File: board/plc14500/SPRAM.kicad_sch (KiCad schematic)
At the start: 26 parts, among them U12 4011, U13 4099, U14 4051

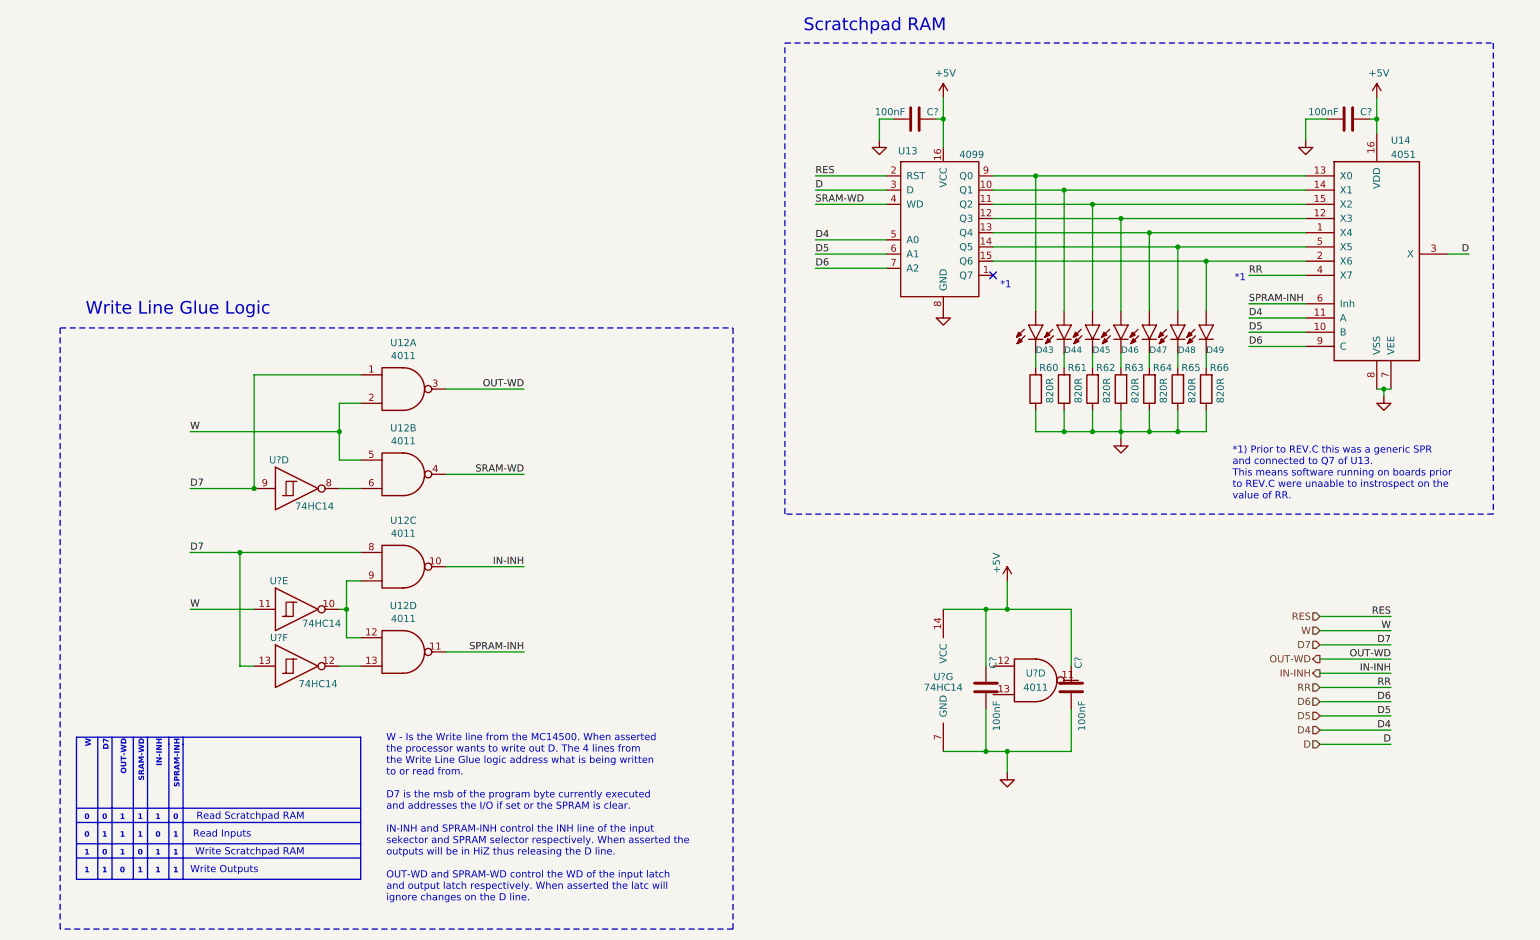
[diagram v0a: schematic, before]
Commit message: Address ERC errors
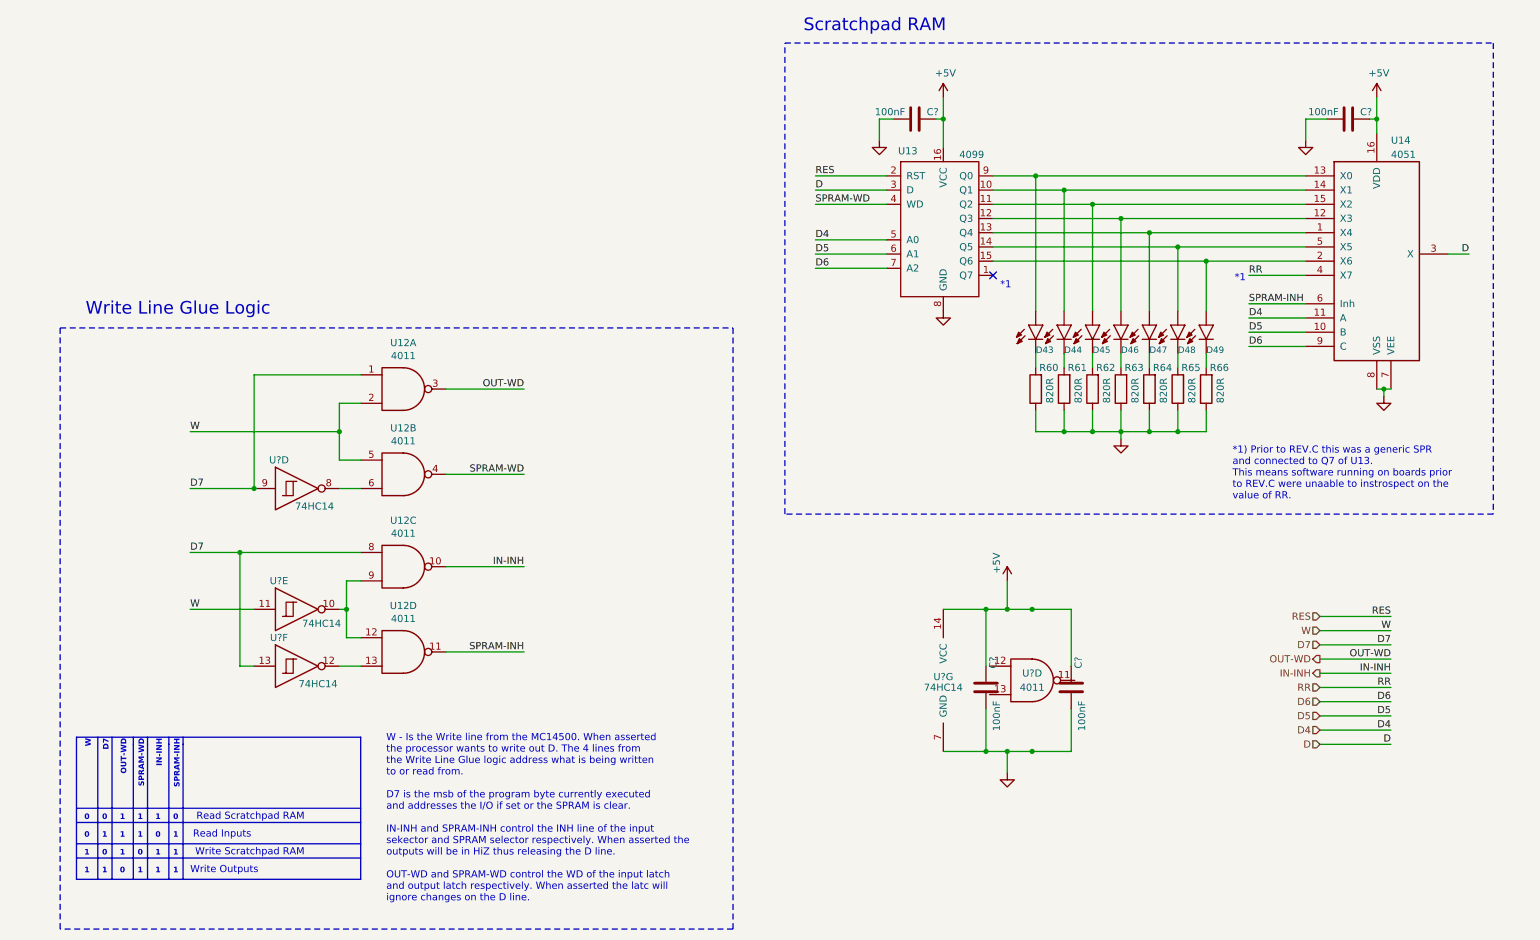
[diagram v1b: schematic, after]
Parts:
- D43, D44, D45, D46, D47, D48, D49: footprint plc14500:LED_3MM -> LED_5MM; symbol plc14500-rescue:LED5MM-SparkFun-LED -> plc14500:LED
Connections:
- net SRAM-WD renamed SPRAM-WD
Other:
- note added: "SPRAM-WD"
- note removed: "SRAM-WD"
- moved on the sheet: U?D
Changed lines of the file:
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@@
     (comment 1 "REV.D")
   )
+  (junction (at 198.755 149.86) (diameter 0) (color 0 0 0 0)
+  )
   (junction (at 214.63 92.71) (diameter 0) (color 0 0 0 0)
   )
@@
   )
   (junction (at 204.47 49.53) (diameter 0) (color 0 0 0 0)
+  )
+  (junction (at 198.755 124.46) (diameter 0) (color 0 0 0 0)
   )
   (junction (at 194.31 124.46) (diameter 0) (color 0 0 0 0)
@@
     (stroke (width 0) (type default))
   )
-  (wire (pts (xy 194.31 124.46) (xy 205.74 124.46))
+  (wire (pts (xy 194.31 124.46) (xy 198.755 124.46))
     (stroke (width 0) (type default))
   )
@@
     (stroke (width 0) (type default))
   )
-  (wire (pts (xy 194.31 149.86) (xy 205.74 149.86))
+  (wire (pts (xy 194.31 149.86) (xy 198.755 149.86))
     (stroke (width 0) (type default))
   )
@@
     (stroke (width 0) (type default))
   )
+  (wire (pts (xy 198.755 124.46) (xy 205.74 124.46))
+    (stroke (width 0) (type default))
+  )
   (wire (pts (xy 93.98 132.08) (xy 107.95 132.08))
     (stroke (width 0) (type default))
   )
   (wire (pts (xy 214.63 54.61) (xy 247.65 54.61))
+    (stroke (width 0) (type default))
+  )
+  (wire (pts (xy 198.755 149.86) (xy 205.74 149.86))
     (stroke (width 0) (type default))
   )
@@
     (effects (font (size 0.9906 0.9906) (thickness 0.1981) bold) (justify right bottom))
   )
-  (text "SRAM-WD" (at 40.132 147.701 90)
+  (text "SPRAM-WD" (at 40.132 147.701 90)
     (effects (font (size 0.9906 0.9906) (thickness 0.1981) bold) (justify right bottom))
   )
@@
     (effects (font (size 1.27 1.27)) (justify right bottom))
   )
-  (label "SRAM-WD" (at 160.02 52.07 0) (fields_autoplaced)
+  (label "SPRAM-WD" (at 160.02 52.07 0) (fields_autoplaced)
     (effects (font (size 1.27 1.27)) (justify left bottom))
   )
@@
     (effects (font (size 1.27 1.27)) (justify right bottom))
   )
-  (label "SRAM-WD" (at 107.95 100.33 180) (fields_autoplaced)
+  (label "SPRAM-WD" (at 107.95 100.33 180) (fields_autoplaced)
     (effects (font (size 1.27 1.27)) (justify right bottom))
   )
@@
     (effects (font (size 1.27 1.27)) (justify right))
   )
-  (symbol (lib_id "plc14500-rescue:LED5MM-SparkFun-LED") (at 199.39 73.66 0) (unit 1)
+  (symbol (lib_id "plc14500:LED") (at 199.39 73.66 0) (unit 1)
     (in_bom yes) (on_board yes) (dnp no)
     (property "Reference" "D43" (at 199.39 78.105 0)
@@
       (effects (font (size 1.143 1.143)) (justify left) hide)
     )
-    (property "Footprint" "plc14500:LED_3MM" (at 194.31 73.66 90)
+    (property "Footprint" "LED_5MM" (at 194.31 73.66 90)
       (effects (font (size 0.508 0.508)) hide)
     )
@@
       (effects (font (size 1.27 1.27)) hide)
     )
-    (property "Field4" "XXX-00000" (at 201.3712 77.0636 0)
-      (effects (font (size 1.524 1.524)) (justify left) hide)
+    (property "Field4" "XXX-00000" (at 193.04 73.66 90)
+      (effects (font (size 1.524 1.524)) hide)
     )
     (property "Price" "0.01" (at 199.39 73.66 0)
@@
     )
   )
-  (symbol (lib_id "plc14500-rescue:LED5MM-SparkFun-LED") (at 204.47 73.66 0) (unit 1)
+  (symbol (lib_id "plc14500:LED") (at 204.47 73.66 0) (unit 1)
     (in_bom yes) (on_board yes) (dnp no)
     (property "Reference" "D44" (at 204.47 78.105 0)
@@
       (effects (font (size 1.143 1.143)) (justify left) hide)
     )
-    (property "Footprint" "plc14500:LED_3MM" (at 199.39 73.66 90)
+    (property "Footprint" "LED_5MM" (at 199.39 73.66 90)
       (effects (font (size 0.508 0.508)) hide)
     )
@@
       (effects (font (size 1.27 1.27)) hide)
     )
-    (property "Field4" "XXX-00000" (at 206.4512 77.0636 0)
-      (effects (font (size 1.524 1.524)) (justify left) hide)
+    (property "Field4" "XXX-00000" (at 198.12 73.66 90)
+      (effects (font (size 1.524 1.524)) hide)
     )
     (property "Price" "0.01" (at 204.47 73.66 0)
@@
     )
   )
-  (symbol (lib_id "plc14500-rescue:LED5MM-SparkFun-LED") (at 209.55 73.66 0) (unit 1)
+  (symbol (lib_id "plc14500:LED") (at 209.55 73.66 0) (unit 1)
     (in_bom yes) (on_board yes) (dnp no)
     (property "Reference" "D45" (at 209.55 78.105 0)
@@
       (effects (font (size 1.143 1.143)) (justify left) hide)
     )
-    (property "Footprint" "plc14500:LED_3MM" (at 204.47 73.66 90)
+    (property "Footprint" "LED_5MM" (at 204.47 73.66 90)
       (effects (font (size 0.508 0.508)) hide)
     )
@@
       (effects (font (size 1.27 1.27)) hide)
     )
-    (property "Field4" "XXX-00000" (at 211.5312 77.0636 0)
-      (effects (font (size 1.524 1.524)) (justify left) hide)
+    (property "Field4" "XXX-00000" (at 203.2 73.66 90)
+      (effects (font (size 1.524 1.524)) hide)
     )
     (property "Price" "0.01" (at 209.55 73.66 0)
@@
     )
   )
-  (symbol (lib_id "plc14500-rescue:LED5MM-SparkFun-LED") (at 214.63 73.66 0) (unit 1)
+  (symbol (lib_id "plc14500:LED") (at 214.63 73.66 0) (unit 1)
     (in_bom yes) (on_board yes) (dnp no)
     (property "Reference" "D46" (at 214.63 78.105 0)
@@
       (effects (font (size 1.143 1.143)) (justify left) hide)
     )
-    (property "Footprint" "plc14500:LED_3MM" (at 209.55 73.66 90)
+    (property "Footprint" "LED_5MM" (at 209.55 73.66 90)
       (effects (font (size 0.508 0.508)) hide)
     )
@@
       (effects (font (size 1.27 1.27)) hide)
     )
-    (property "Field4" "XXX-00000" (at 216.6112 77.0636 0)
-      (effects (font (size 1.524 1.524)) (justify left) hide)
+    (property "Field4" "XXX-00000" (at 208.28 73.66 90)
+      (effects (font (size 1.524 1.524)) hide)
     )
     (property "Price" "0.01" (at 214.63 73.66 0)
@@
     )
   )
-  (symbol (lib_id "plc14500-rescue:LED5MM-SparkFun-LED") (at 219.71 73.66 0) (unit 1)
+  (symbol (lib_id "plc14500:LED") (at 219.71 73.66 0) (unit 1)
     (in_bom yes) (on_board yes) (dnp no)
     (property "Reference" "D47" (at 219.71 78.105 0)
@@
       (effects (font (size 1.143 1.143)) (justify left) hide)
     )
-    (property "Footprint" "plc14500:LED_3MM" (at 214.63 73.66 90)
+    (property "Footprint" "LED_5MM" (at 214.63 73.66 90)
       (effects (font (size 0.508 0.508)) hide)
     )
@@
       (effects (font (size 1.27 1.27)) hide)
     )
-    (property "Field4" "XXX-00000" (at 221.6912 77.0636 0)
-      (effects (font (size 1.524 1.524)) (justify left) hide)
+    (property "Field4" "XXX-00000" (at 213.36 73.66 90)
+      (effects (font (size 1.524 1.524)) hide)
     )
     (property "Price" "0.01" (at 219.71 73.66 0)
@@
     )
   )
-  (symbol (lib_id "plc14500-rescue:LED5MM-SparkFun-LED") (at 224.79 73.66 0) (unit 1)
+  (symbol (lib_id "plc14500:LED") (at 224.79 73.66 0) (unit 1)
     (in_bom yes) (on_board yes) (dnp no)
     (property "Reference" "D48" (at 224.79 78.105 0)
@@
       (effects (font (size 1.143 1.143)) (justify left) hide)
     )
-    (property "Footprint" "plc14500:LED_3MM" (at 219.71 73.66 90)
+    (property "Footprint" "LED_5MM" (at 219.71 73.66 90)
       (effects (font (size 0.508 0.508)) hide)
     )
@@
       (effects (font (size 1.27 1.27)) hide)
     )
-    (property "Field4" "XXX-00000" (at 226.7712 77.0636 0)
-      (effects (font (size 1.524 1.524)) (justify left) hide)
+    (property "Field4" "XXX-00000" (at 218.44 73.66 90)
+      (effects (font (size 1.524 1.524)) hide)
     )
     (property "Price" "0.01" (at 224.79 73.66 0)
@@
     )
   )
-  (symbol (lib_id "plc14500-rescue:LED5MM-SparkFun-LED") (at 229.87 73.66 0) (unit 1)
+  (symbol (lib_id "plc14500:LED") (at 229.87 73.66 0) (unit 1)
     (in_bom yes) (on_board yes) (dnp no)
     (property "Reference" "D49" (at 229.87 78.105 0)
@@
       (effects (font (size 1.143 1.143)) (justify left) hide)
     )
-    (property "Footprint" "plc14500:LED_3MM" (at 224.79 73.66 90)
+    (property "Footprint" "LED_5MM" (at 224.79 73.66 90)
       (effects (font (size 0.508 0.508)) hide)
     )
@@
       (effects (font (size 1.27 1.27)) hide)
     )
-    (property "Field4" "XXX-00000" (at 231.8512 77.0636 0)
-      (effects (font (size 1.524 1.524)) (justify left) hide)
+    (property "Field4" "XXX-00000" (at 223.52 73.66 90)
+      (effects (font (size 1.524 1.524)) hide)
     )
     (property "Price" "0.01" (at 229.87 73.66 0)
@@
     )
   )
-  (symbol (lib_id "plc14500:4011") (at 199.39 137.16 0) (unit 4)
-    (in_bom yes) (on_board yes) (dnp no)
-    (property "Reference" "U?" (at 199.39 135.89 0)
-      (effects (font (size 1.27 1.27)))
-    )
-    (property "Value" "4011" (at 199.39 138.43 0)
-      (effects (font (size 1.27 1.27)))
-    )
-    (property "Footprint" "Package_DIP:DIP-14_W7.62mm_LongPads" (at 199.39 137.16 0)
-      (effects (font (size 1.27 1.27)) hide)
-    )
-    (property "Datasheet" "http://www.intersil.com/content/dam/Intersil/documents/cd40/cd4011bms-12bms-23bms.pdf" (at 199.39 137.16 0)
-      (effects (font (size 1.27 1.27)) hide)
-    )
-    (property "Price" "0.2" (at 199.39 137.16 0)
-      (effects (font (size 1.27 1.27)) hide)
-    )
+  (symbol (lib_id "plc14500:4011") (at 198.755 137.16 0) (unit 4)
+    (in_bom yes) (on_board yes) (dnp no)
+    (property "Reference" "U?" (at 198.755 135.89 0)
+      (effects (font (size 1.27 1.27)))
+    )
+    (property "Value" "4011" (at 198.755 138.43 0)
+      (effects (font (size 1.27 1.27)))
+    )
+    (property "Footprint" "Package_DIP:DIP-14_W7.62mm_LongPads" (at 198.755 137.16 0)
+      (effects (font (size 1.27 1.27)) hide)
+    )
+    (property "Datasheet" "http://www.intersil.com/content/dam/Intersil/documents/cd40/cd4011bms-12bms-23bms.pdf" (at 198.755 137.16 0)
+      (effects (font (size 1.27 1.27)) hide)
+    )
+    (property "Price" "0.2" (at 198.755 137.16 0)
+      (effects (font (size 1.27 1.27)) hide)
+    )

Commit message: Cleanup, ready to route
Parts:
- D43, D44, D45, D46, D47, D48, D49: footprint LED_5MM -> plc14500:LED_3MM; Field4 XXX-00000 -> (none)
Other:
- moved on the sheet: U?D
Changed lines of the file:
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@@
     (comment 1 "REV.D")
   )
-  (junction (at 198.755 149.86) (diameter 0) (color 0 0 0 0)
-  )
   (junction (at 214.63 92.71) (diameter 0) (color 0 0 0 0)
   )
@@
   (junction (at 190.5 124.46) (diameter 0) (color 0 0 0 0)
   )
+  (junction (at 199.39 149.86) (diameter 0) (color 0 0 0 0)
+  )
   (junction (at 224.79 59.69) (diameter 0) (color 0 0 0 0)
   )
@@
   (junction (at 209.55 92.71) (diameter 0) (color 0 0 0 0)
   )
+  (junction (at 199.39 124.46) (diameter 0) (color 0 0 0 0)
+  )
   (junction (at 182.88 36.83) (diameter 0) (color 0 0 0 0)
   )
@@
   )
   (junction (at 204.47 49.53) (diameter 0) (color 0 0 0 0)
-  )
-  (junction (at 198.755 124.46) (diameter 0) (color 0 0 0 0)
   )
   (junction (at 194.31 124.46) (diameter 0) (color 0 0 0 0)
@@
     (stroke (width 0) (type default))
   )
+  (wire (pts (xy 199.39 149.86) (xy 205.74 149.86))
+    (stroke (width 0) (type default))
+  )
   (wire (pts (xy 59.69 82.55) (xy 59.69 102.87))
     (stroke (width 0) (type default))
@@
     (stroke (width 0) (type default))
   )
-  (wire (pts (xy 194.31 124.46) (xy 198.755 124.46))
+  (wire (pts (xy 194.31 124.46) (xy 199.39 124.46))
     (stroke (width 0) (type default))
   )
@@
     (stroke (width 0) (type default))
   )
-  (wire (pts (xy 194.31 149.86) (xy 198.755 149.86))
+  (wire (pts (xy 194.31 149.86) (xy 199.39 149.86))
     (stroke (width 0) (type default))
   )
@@
     (stroke (width 0) (type default))
   )
-  (wire (pts (xy 198.755 124.46) (xy 205.74 124.46))
-    (stroke (width 0) (type default))
-  )
   (wire (pts (xy 93.98 132.08) (xy 107.95 132.08))
     (stroke (width 0) (type default))
@@
     (stroke (width 0) (type default))
   )
-  (wire (pts (xy 198.755 149.86) (xy 205.74 149.86))
-    (stroke (width 0) (type default))
-  )
   (polyline (pts (xy 46.99 147.32) (xy 46.99 148.59))
     (stroke (width 0) (type default))
@@
   )
   (wire (pts (xy 229.87 78.74) (xy 229.87 81.28))
+    (stroke (width 0) (type default))
+  )
+  (wire (pts (xy 199.39 124.46) (xy 205.74 124.46))
     (stroke (width 0) (type default))
   )
@@
       (effects (font (size 1.143 1.143)) (justify left) hide)
     )
-    (property "Footprint" "LED_5MM" (at 194.31 73.66 90)
+    (property "Footprint" "plc14500:LED_3MM" (at 194.31 73.66 90)
       (effects (font (size 0.508 0.508)) hide)
     )
@@
       (effects (font (size 1.27 1.27)) hide)
     )
-    (property "Field4" "XXX-00000" (at 193.04 73.66 90)
+    (property "Field4" "" (at 193.04 73.66 90)
       (effects (font (size 1.524 1.524)) hide)
     )
@@
       (effects (font (size 1.143 1.143)) (justify left) hide)
     )
-    (property "Footprint" "LED_5MM" (at 199.39 73.66 90)
+    (property "Footprint" "plc14500:LED_3MM" (at 199.39 73.66 90)
       (effects (font (size 0.508 0.508)) hide)
     )
@@
       (effects (font (size 1.27 1.27)) hide)
     )
-    (property "Field4" "XXX-00000" (at 198.12 73.66 90)
+    (property "Field4" "" (at 198.12 73.66 90)
       (effects (font (size 1.524 1.524)) hide)
     )
@@
       (effects (font (size 1.143 1.143)) (justify left) hide)
     )
-    (property "Footprint" "LED_5MM" (at 204.47 73.66 90)
+    (property "Footprint" "plc14500:LED_3MM" (at 204.47 73.66 90)
       (effects (font (size 0.508 0.508)) hide)
     )
@@
       (effects (font (size 1.27 1.27)) hide)
     )
-    (property "Field4" "XXX-00000" (at 203.2 73.66 90)
+    (property "Field4" "" (at 203.2 73.66 90)
       (effects (font (size 1.524 1.524)) hide)
     )
@@
       (effects (font (size 1.143 1.143)) (justify left) hide)
     )
-    (property "Footprint" "LED_5MM" (at 209.55 73.66 90)
+    (property "Footprint" "plc14500:LED_3MM" (at 209.55 73.66 90)
       (effects (font (size 0.508 0.508)) hide)
     )
@@
       (effects (font (size 1.27 1.27)) hide)
     )
-    (property "Field4" "XXX-00000" (at 208.28 73.66 90)
+    (property "Field4" "" (at 208.28 73.66 90)
       (effects (font (size 1.524 1.524)) hide)
     )
@@
       (effects (font (size 1.143 1.143)) (justify left) hide)
     )
-    (property "Footprint" "LED_5MM" (at 214.63 73.66 90)
+    (property "Footprint" "plc14500:LED_3MM" (at 214.63 73.66 90)
       (effects (font (size 0.508 0.508)) hide)
     )
@@
       (effects (font (size 1.27 1.27)) hide)
     )
-    (property "Field4" "XXX-00000" (at 213.36 73.66 90)
+    (property "Field4" "" (at 213.36 73.66 90)
       (effects (font (size 1.524 1.524)) hide)
     )
@@
       (effects (font (size 1.143 1.143)) (justify left) hide)
     )
-    (property "Footprint" "LED_5MM" (at 219.71 73.66 90)
+    (property "Footprint" "plc14500:LED_3MM" (at 219.71 73.66 90)
       (effects (font (size 0.508 0.508)) hide)
     )
@@
       (effects (font (size 1.27 1.27)) hide)
     )
-    (property "Field4" "XXX-00000" (at 218.44 73.66 90)
+    (property "Field4" "" (at 218.44 73.66 90)
       (effects (font (size 1.524 1.524)) hide)
     )
@@
       (effects (font (size 1.143 1.143)) (justify left) hide)
     )
-    (property "Footprint" "LED_5MM" (at 224.79 73.66 90)
+    (property "Footprint" "plc14500:LED_3MM" (at 224.79 73.66 90)
       (effects (font (size 0.508 0.508)) hide)
     )
@@
       (effects (font (size 1.27 1.27)) hide)
     )
-    (property "Field4" "XXX-00000" (at 223.52 73.66 90)
+    (property "Field4" "" (at 223.52 73.66 90)
       (effects (font (size 1.524 1.524)) hide)
     )
@@
         )
         (path "/e5c24396-229a-4727-a88d-8f28d7f70179/00000000-0000-0000-0000-000067425b3b"
-          (reference "C15") (unit 1)
-        )
-      )
-    )
-  )
-  (symbol (lib_id "plc14500:4011") (at 198.755 137.16 0) (unit 4)
-    (in_bom yes) (on_board yes) (dnp no)
-    (property "Reference" "U?" (at 198.755 135.89 0)
-      (effects (font (size 1.27 1.27)))
-    )
-    (property "Value" "4011" (at 198.755 138.43 0)
-      (effects (font (size 1.27 1.27)))
-    )
-    (property "Footprint" "Package_DIP:DIP-14_W7.62mm_LongPads" (at 198.755 137.16 0)
-      (effects (font (size 1.27 1.27)) hide)
-    )
-    (property "Datasheet" "http://www.intersil.com/content/dam/Intersil/documents/cd40/cd4011bms-12bms-23bms.pdf" (at 198.755 137.16 0)
-      (effects (font (size 1.27 1.27)) hide)
-    )
-    (property "Price" "0.2" (at 198.755 137.16 0)
-      (effects (font (size 1.27 1.27)) hide)
-    )
+          (reference "C19") (unit 1)
+        )
+      )
+    )
+  )
+  (symbol (lib_id "plc14500:4011") (at 199.39 137.16 0) (unit 4)
+    (in_bom yes) (on_board yes) (dnp no)
+    (property "Reference" "U?" (at 199.39 135.89 0)
+      (effects (font (size 1.27 1.27)))
+    )
+    (property "Value" "4011" (at 199.39 138.43 0)
+      (effects (font (size 1.27 1.27)))
+    )
+    (property "Footprint" "Package_DIP:DIP-14_W7.62mm_LongPads" (at 199.39 137.16 0)
+      (effects (font (size 1.27 1.27)) hide)
+    )
+    (property "Datasheet" "http://www.intersil.com/content/dam/Intersil/documents/cd40/cd4011bms-12bms-23bms.pdf" (at 199.39 137.16 0)
+      (effects (font (size 1.27 1.27)) hide)
+    )
+    (property "Price" "0.2" (at 199.39 137.16 0)
+      (effects (font (size 1.27 1.27)) hide)
+    )
